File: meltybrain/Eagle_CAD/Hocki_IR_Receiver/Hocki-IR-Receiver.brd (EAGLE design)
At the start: 36 x 34 mm, 67 parts, among them U1 OPA2380AIDGKR, U10 LMH6612MAX/NOPB, U11 LMH6612MAX/NOPB, U2 OPA2380AIDGKR, U3 TLV3502AIDCNR, U4 TLV3502AIDCNR, U5 SN74LVC1G58DCKR, U6 NL27WZ32USG, U7 TMUX1204DGSR, U8 LP38693MP-5.0/NOPB, U9 TLV73310PDBVT

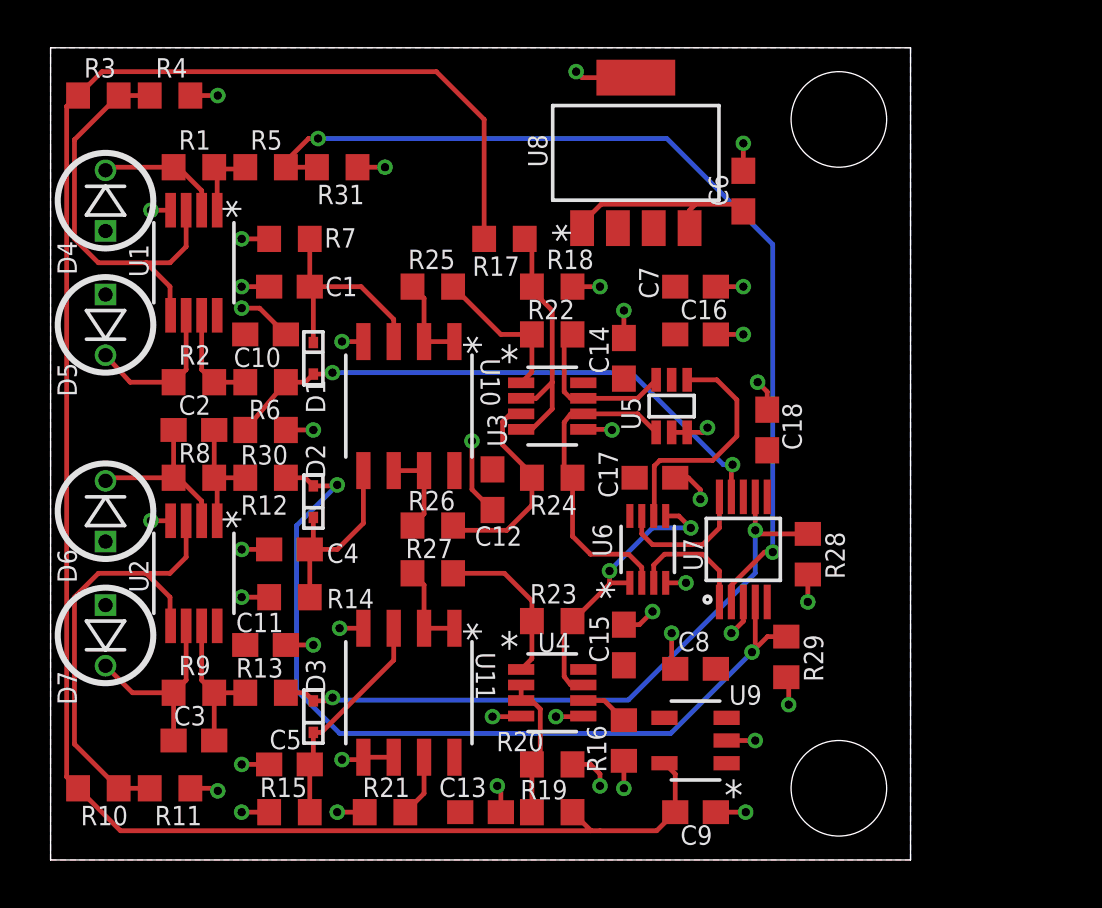
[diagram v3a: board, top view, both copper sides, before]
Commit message: updates
IR receiver should only be missing the connector
started layout for control...gave up...too late
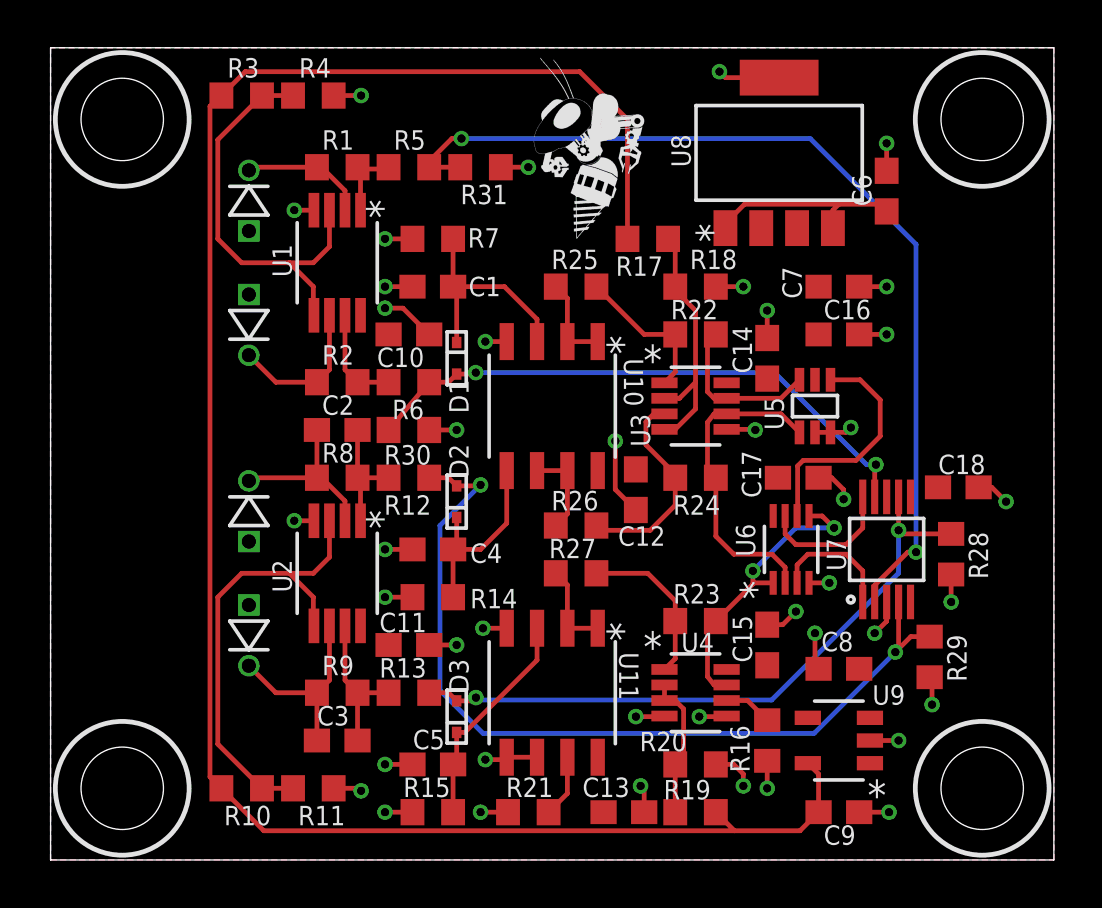
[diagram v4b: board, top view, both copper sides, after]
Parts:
- added U$1: (no value), RoboJackets-Aesthetics:ROBOBUZZ_0.4X
- added U$2: (no value), RoboJackets-Aesthetics:ROBOJACKETS
- moved C18 8.35 mm to (38.0, 15.6), turned to 0 degrees
- moved R28 6.00 mm to (37.7, 12.8)
- moved D4 6.00 mm to (8.30, 27.6), flipped to the bottom
- moved D5 6.00 mm to (8.30, 22.4), flipped to the bottom
- moved D6 6.00 mm to (8.30, 14.6), flipped to the bottom
- moved D7 6.00 mm to (8.30, 9.40), flipped to the bottom
- moved C1 6.00 mm to (16.0, 24.0)
- moved C10 6.00 mm to (15.0, 22.0)
- moved C11 6.00 mm to (15.0, 9.00)
- moved C12 6.00 mm to (24.5, 15.5)
- moved C13 6.00 mm to (24.0, 2.00)
- moved C14 6.00 mm to (30.0, 21.0)
- moved C15 6.00 mm to (30.0, 9.00)
- moved C16 6.00 mm to (33.0, 22.0)
- moved C17 6.00 mm to (31.3, 16.0)
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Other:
- board size 36 x 34 mm -> 42 x 34 mm
- board text added: "IR Receiver V1"

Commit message: progress...
IR receiver has all parts accounting BoM
started doing that for control
progress on control layout
Varun I hate this...
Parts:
- removed C4, C5: 50n, rcl:C0603
- removed R5: 50, resistor:R0603
- C1: value 50n -> 47n; device rcl:C0603 -> rcl:C1206
- C2: value 0.5p -> 47n; device rcl:C0603 -> rcl:C1206
- C3: value 2p -> 47n; device rcl:C0603 -> rcl:C1206
- R1: device resistor:R0603 -> rcl:R1206
- R10, R11, R16, R21, R28, R29, R3, R30, R31, R4: value 500 -> 499
- R14, R15, R7: value 30k -> 31.6k
- moved C2 7.07 mm to (17.0, 13.0), turned to 180 degrees
- moved R30 3.00 mm to (12.0, 18.0), turned to 0 degrees
- moved C1 2.00 mm to (18.0, 24.0)
- moved C3 2.00 mm to (14.0, 5.00), turned to 180 degrees
- moved R15 1.41 mm to (15.0, 3.00)
- moved R1 1.00 mm to (13.0, 29.0)
- moved R31 1.00 mm to (17.0, 29.0)
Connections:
- removed net N$11: C3.2, R13.1, R9.2, U2.7
- removed net N$8: C2.2, R12.1, R8.2, U2.1
- new net N$21: D1.2, R6.2
- net 100KGAIN: now also R12.1, R8.2, U2.1; no longer D2.2, R12.2
- net 100KPEAK: now also C2.1; no longer C4.1
- net 10KGAIN: now also R13.1, R9.2, U2.7; no longer D3.2, R13.2
- net 10KPEAK: now also C3.1; no longer C5.1
- net 10MGAIN: now also R1.2, U1.1; no longer R5.2
- net 1MGAIN: now also R2.2, R6.1, U1.7; no longer D1.2, R6.2
- net GND: now also C2.2, C3.2; no longer C4.2, C5.2
- net N$10: no longer C3.1
- net N$2: now also D2.2, R12.2; no longer R1.2, R5.1, U1.1
- net N$4: now also D3.2, R13.2; no longer R2.2, R6.1, U1.7
- net N$6: no longer C2.1
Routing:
- net N$11: track 6.32 -> 0.00 mm
- net 1MGAIN: track 24.5 -> 30.6 mm
- net 10KGAIN: track 27.5 -> 33.2 mm
- net N$8: track 5.15 -> 0.00 mm
- net N$4: track 4.32 -> 1.29 mm
- net 10MGAIN: track 40.4 -> 42.7 mm
- net N$10: track 8.34 -> 6.34 mm
- net N$6: track 7.31 -> 5.31 mm
- net N$2: track 3.11 -> 1.29 mm
- net 100KGAIN: track 36.7 -> 38.4 mm
- net GND: track 56.0 -> 57.7 mm
- net N$21: track 0.00 -> 1.29 mm
- net 10KPEAK: track 9.36 -> 9.88 mm

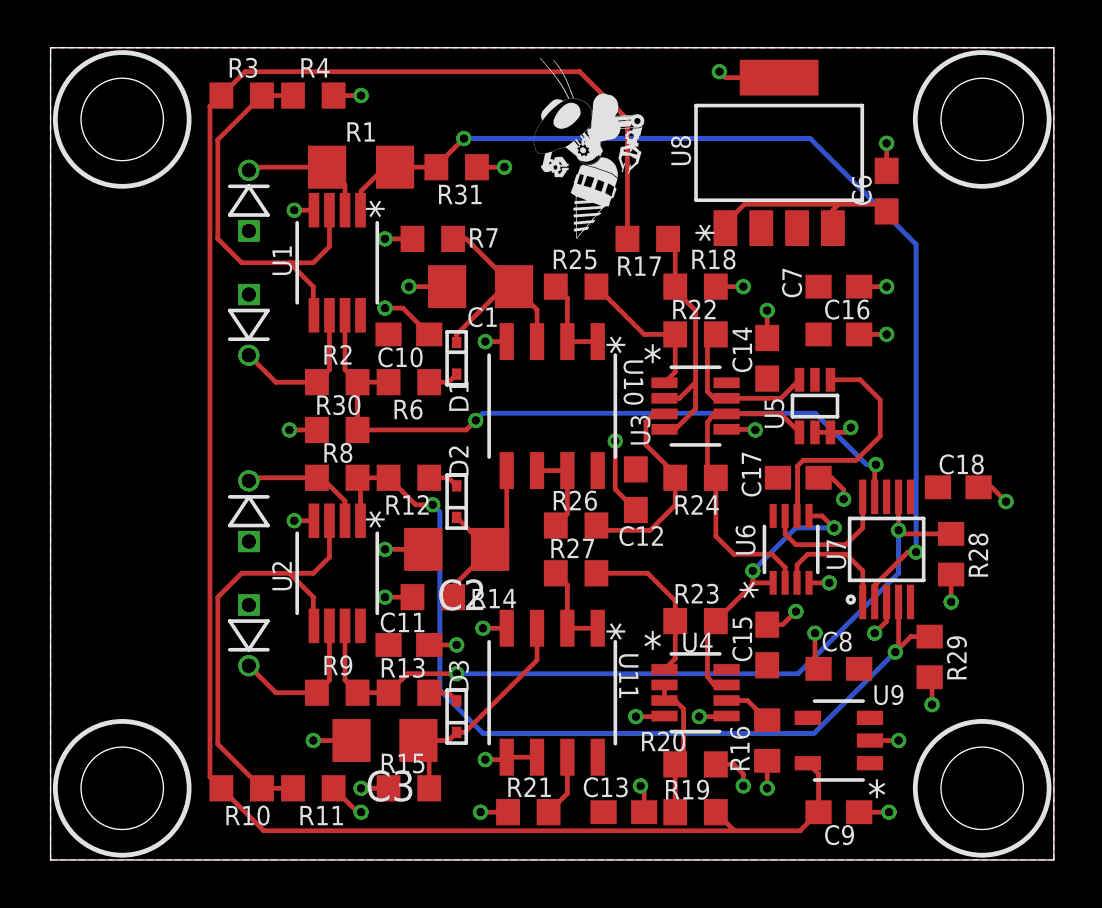
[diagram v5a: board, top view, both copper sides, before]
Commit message: added IR connectors
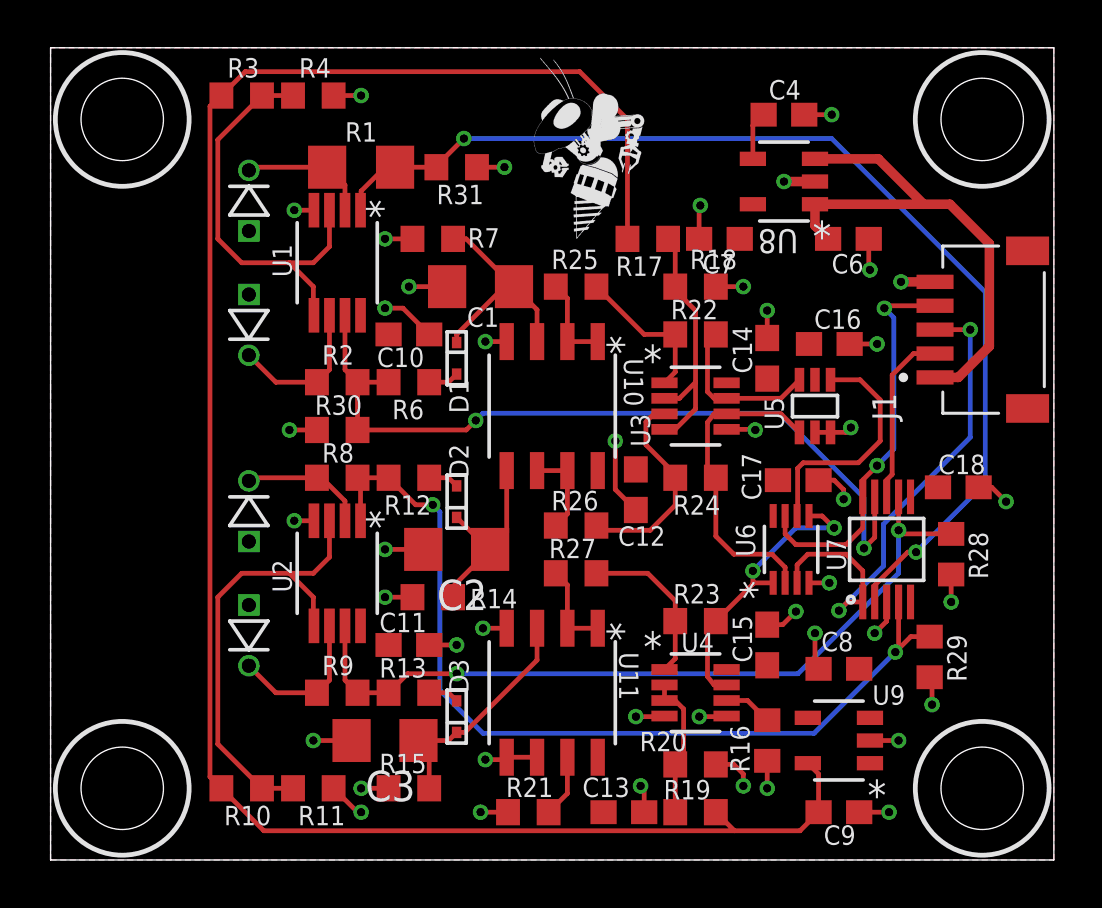
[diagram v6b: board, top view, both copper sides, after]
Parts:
- added C4: 100p, rcl:C0603
- added J1: SM05B-SRSS-TB(LF)(SN), Hocki_Library:SM05B-SRSS-TB(LF)(SN)
- C7: value 1u -> 2.2u
- U8: value LP38693MP-5.0/NOPB -> AP2210K-5.0TRG1; device Hocki_Library:SOT-223-5 -> Hocki_Library:SOT-23-5
- moved C7 5.39 mm to (28.0, 26.0), turned to 180 degrees
- moved C6 2.56 mm to (33.4, 26.0), turned to 0 degrees
- moved U8 1.22 mm to (30.7, 28.4), turned to 180 degrees
- moved C16 0.57 mm to (32.6, 21.6)
- moved C17 0.10 mm to (31.3, 15.9)
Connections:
- removed net VIN: C6.1, U8.1, U8.4
- new net 9V: C6.1, J1.1, U8.1, U8.3
- new net N$8: C4.1, U8.4
- net 5V: now also J1.S1, J1.S2, U8.5; no longer U8.3
- net A0: now also J1.3
- net A1: now also J1.4
- net GND: now also C4.2, J1.5, U8.2; no longer U8.5
- net VG_SIGNAL: now also J1.2
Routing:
- net 9V: track 0.00 -> 22.1 mm
- net A0: track 5.28 -> 21.9 mm, vias 0 -> 2
- net A1: track 5.78 -> 16.5 mm, vias 0 -> 2
- net VIN: track 8.51 -> 0.00 mm
- net VG_SIGNAL: track 0.00 -> 7.36 mm
- net 1MGAIN: track 30.6 -> 33.7 mm
- net 10MGAIN: track 42.7 -> 45.6 mm
- net N$8: track 0.00 -> 2.04 mm
- net GND: track 57.7 -> 59.4 mm, vias 42 -> 44

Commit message: 5 to 3 pin connector
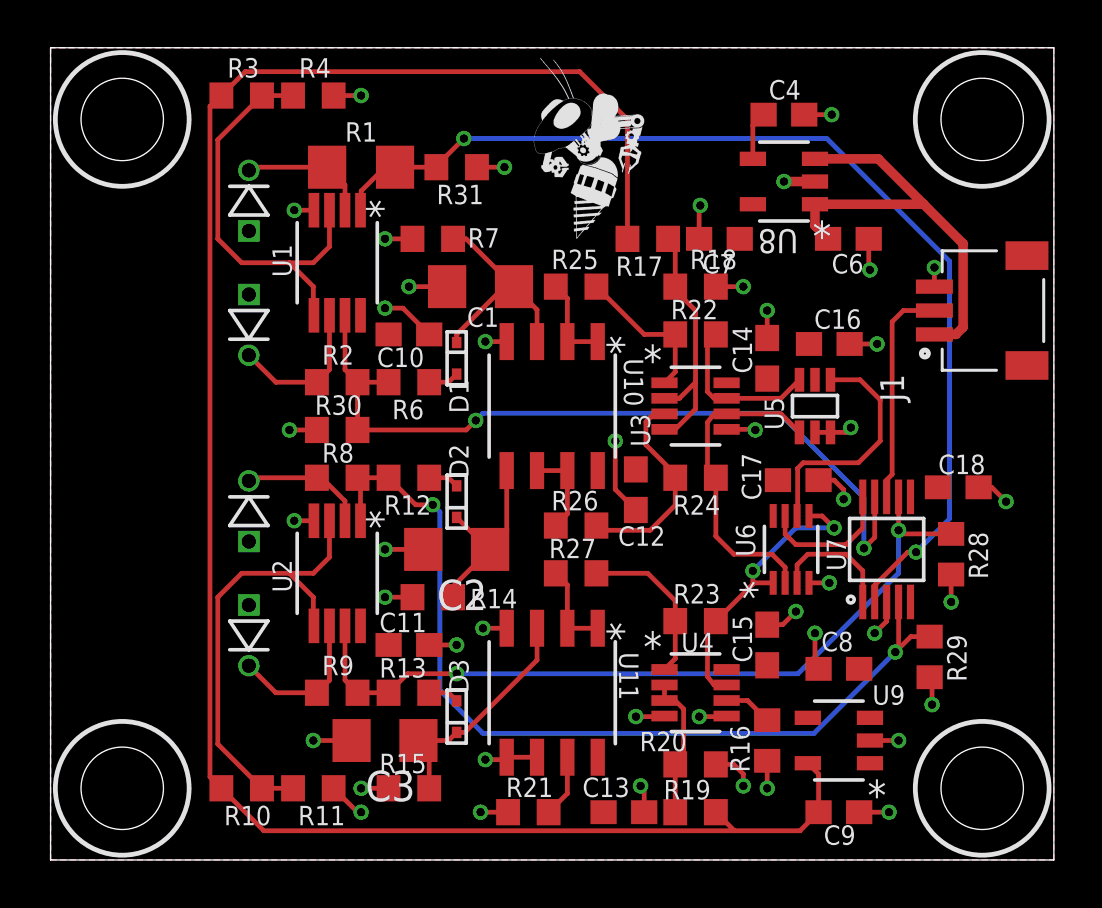
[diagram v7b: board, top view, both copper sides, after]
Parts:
- J1: value SM05B-SRSS-TB(LF)(SN) -> SM03B-SRSS-TB(LF)(SN); device Hocki_Library:SM05B-SRSS-TB(LF)(SN) -> Hocki_Library:SM03B-SRSS-TB(LF)(SN)
- moved J1 3.98 mm to (37.0, 23.0)
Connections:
- net A0: no longer J1.3
- net A1: no longer J1.4
- net GND: now also J1.3; no longer J1.5
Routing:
- net A0: track 21.9 -> 5.28 mm, vias 2 -> 0
- net A1: track 16.5 -> 5.78 mm, vias 2 -> 0
- net 9V: track 22.1 -> 18.7 mm
- net VG_SIGNAL: track 7.36 -> 9.39 mm
- net 10MGAIN: track 45.6 -> 44.3 mm
- net GND: track 59.4 -> 58.7 mm
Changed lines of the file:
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@@
 <attribute name="VALUE" x="30.065" y="29.295" size="1.27" layer="27"/>
 </element>
-<element name="J1" library="Hocki_Library" package="SM05B-SRSS-TB(LF)(SN)" value="SM05B-SRSS-TB(LF)(SN)" x="40.9" y="22.2" smashed="yes" rot="R90">
-<attribute name="DKPN" value="455-1805-1-ND" x="40.9" y="22.2" size="1.778" layer="27" rot="R90" display="off"/>
-<attribute name="NAME" x="35.4" y="18.4" size="1" layer="25" font="vector" rot="R90"/>
-<attribute name="VALUE" x="42.4" y="18.7" size="1" layer="27" font="vector" rot="R90" align="top-left"/>
+<element name="J1" library="Hocki_Library" package="SM03B-SRSS-TB(LF)(SN)" value="SM03B-SRSS-TB(LF)(SN)" x="37" y="23" smashed="yes" rot="R90">
+<attribute name="DKPN" value="455-1803-1-ND" x="37" y="23" size="1.778" layer="27" rot="R90" display="off"/>
+<attribute name="NAME" x="35.73" y="19.19" size="1" layer="25" font="vector" rot="R90"/>
+<attribute name="VALUE" x="42.35" y="19.19" size="1" layer="27" font="vector" rot="R90" align="top-left"/>
 </element>
 </elements>
@@
 <wire x1="32" y1="28.4" x2="30.7" y2="28.4" width="0.4" layer="1"/>
 <via x="30.7" y="28.4" extent="1-16" drill="0.35"/>
-<contactref element="J1" pad="5"/>
-<wire x1="37.025" y1="24.2" x2="35.6" y2="24.2" width="0.4" layer="1"/>
-<via x="35.6" y="24.2" extent="1-16" drill="0.35"/>
+<contactref element="J1" pad="3"/>
+<wire x1="37" y1="24" x2="37" y2="24.8" width="0.2" layer="1"/>
+<via x="37" y="24.8" extent="1-16" drill="0.35"/>
 </signal>
 <signal name="5V">
@@
 <contactref element="C18" pad="1"/>
 <contactref element="U8" pad="5"/>
+<contactref element="J1" pad="S2"/>
 <contactref element="J1" pad="S1"/>
-<contactref element="J1" pad="S2"/>
 </signal>
 <signal name="1MGAIN">
@@
 <wire x1="35.88615" y1="12.88615" x2="36.2306" y2="12.88615" width="0.2" layer="1"/>
 <via x="36.2306" y="12.88615" extent="1-16" drill="0.35"/>
-<wire x1="36.2306" y1="12.88615" x2="39.1306" y2="15.78615" width="0.2" layer="16"/>
-<wire x1="39.1306" y1="23.7694" x2="39.1306" y2="15.78615" width="0.2" layer="16"/>
-<wire x1="32.7" y1="30.2" x2="17.3" y2="30.2" width="0.2" layer="16"/>
+<wire x1="36.2306" y1="12.88615" x2="37.6306" y2="14.28615" width="0.2" layer="16"/>
+<wire x1="37.6306" y1="25.0694" x2="37.6306" y2="14.28615" width="0.2" layer="16"/>
+<wire x1="32.5" y1="30.2" x2="17.3" y2="30.2" width="0.2" layer="16"/>
 <via x="17.3" y="30.2" extent="1-16" drill="0.35"/>
 <wire x1="17.3" y1="30.2" x2="16.15" y2="29.05" width="0.2" layer="1"/>
 <wire x1="16.15" y1="29" x2="16.15" y2="29.05" width="0.2" layer="1"/>
 <wire x1="34.5" y1="11.5" x2="35.88615" y2="12.88615" width="0.2" layer="1"/>
-<wire x1="39.1306" y1="23.7694" x2="32.7" y2="30.2" width="0.2" layer="16"/>
+<wire x1="37.6306" y1="25.0694" x2="32.5" y2="30.2" width="0.2" layer="16"/>
 <contactref element="R31" pad="2"/>
 <contactref element="U1" pad="1"/>
@@
 <wire x1="34" y1="13.9" x2="33.3" y2="13.2" width="0.2" layer="1"/>
 <wire x1="34" y1="15.2" x2="34" y2="13.9" width="0.2" layer="1"/>
-<wire x1="34" y1="15.2" x2="34" y2="15.9064" width="0.2" layer="1"/>
-<wire x1="34" y1="15.9064" x2="34.6" y2="16.5064" width="0.2" layer="1"/>
-<via x="34.6" y="16.5064" extent="1-16" drill="0.35"/>
-<via x="34.904096875" y="23.095903125" extent="1-16" drill="0.35"/>
-<wire x1="34.904096875" y1="23.095903125" x2="35.3" y2="22.7" width="0.2" layer="16"/>
-<wire x1="34.6" y1="16.5064" x2="35.3" y2="17.2064" width="0.2" layer="16"/>
-<wire x1="35.3" y1="22.7" x2="35.3" y2="17.2064" width="0.2" layer="16"/>
-<contactref element="J1" pad="4"/>
-<wire x1="34.904096875" y1="23.095903125" x2="35.00819375" y2="23.2" width="0.2" layer="1"/>
-<wire x1="35.00819375" y1="23.2" x2="37.025" y2="23.2" width="0.2" layer="1"/>
 </signal>
 <signal name="A0">
@@
 <wire x1="33.3" y1="12.8" x2="34" y2="12.1" width="0.2" layer="1"/>
 <wire x1="34" y1="12.1" x2="34" y2="10.8" width="0.2" layer="1"/>
-<contactref element="J1" pad="3"/>
-<wire x1="34" y1="10.8" x2="33.3628" y2="10.8" width="0.2" layer="1"/>
-<wire x1="33.3628" y1="10.8" x2="33" y2="10.4372" width="0.2" layer="1"/>
-<via x="33" y="10.4372" extent="1-16" drill="0.35"/>
-<via x="38.5" y="22.2" extent="1-16" drill="0.35"/>
-<wire x1="33" y1="10.4372" x2="34.8694" y2="12.3066" width="0.2" layer="16"/>
-<wire x1="38.5" y1="17.69180625" x2="38.5" y2="22.2" width="0.2" layer="16"/>
-<wire x1="34.8694" y1="12.3066" x2="34.8694" y2="14.06120625" width="0.2" layer="16"/>
-<wire x1="34.8694" y1="14.06120625" x2="38.5" y2="17.69180625" width="0.2" layer="16"/>
-<wire x1="37.025" y1="22.2" x2="38.5" y2="22.2" width="0.2" layer="1"/>
 </signal>
 <signal name="N$13">
@@
 <wire x1="35" y1="15.2" x2="35" y2="15.90819375" width="0.2" layer="1"/>
 <wire x1="35" y1="15.90819375" x2="35.2306" y2="16.13879375" width="0.2" layer="1"/>
-<wire x1="35.2306" y1="16.13879375" x2="35.2306" y2="20.3" width="0.2" layer="1"/>
+<wire x1="35.2306" y1="16.13879375" x2="35.2306" y2="22.5306" width="0.2" layer="1"/>
 <contactref element="J1" pad="2"/>
-<wire x1="37.025" y1="21.2" x2="36.1306" y2="21.2" width="0.2" layer="1"/>
-<wire x1="36.1306" y1="21.2" x2="35.2306" y2="20.3" width="0.2" layer="1"/>
+<wire x1="37" y1="23" x2="35.7" y2="23" width="0.2" layer="1"/>
+<wire x1="35.7" y1="23" x2="35.2306" y2="22.5306" width="0.2" layer="1"/>
 </signal>
 <signal name="N$17">
@@
 <contactref element="U8" pad="1"/>
 <contactref element="U8" pad="3"/>
-<contactref element="J1" pad="1"/>
-<wire x1="37.025" y1="20.2" x2="38" y2="20.2" width="0.4" layer="1"/>
-<wire x1="38" y1="20.2" x2="39.3" y2="21.5" width="0.4" layer="1"/>
-<wire x1="39.3" y1="21.5" x2="39.3" y2="25.8" width="0.4" layer="1"/>
+<wire x1="38.2" y1="22.3" x2="38.2" y2="25.8" width="0.4" layer="1"/>
 <wire x1="32" y1="27.45" x2="36.55" y2="27.45" width="0.4" layer="1"/>
-<wire x1="36.55" y1="27.45" x2="37.65" y2="27.45" width="0.4" layer="1"/>
-<wire x1="39.3" y1="25.8" x2="37.65" y2="27.45" width="0.4" layer="1"/>
+<wire x1="38.2" y1="25.8" x2="36.55" y2="27.45" width="0.4" layer="1"/>
 <wire x1="32.55" y1="26" x2="32" y2="26.55" width="0.4" layer="1"/>
 <wire x1="32" y1="26.55" x2="32" y2="27.45" width="0.4" layer="1"/>
 <wire x1="36.55" y1="27.45" x2="34.65" y2="29.35" width="0.4" layer="1"/>
 <wire x1="34.65" y1="29.35" x2="32" y2="29.35" width="0.4" layer="1"/>
+<contactref element="J1" pad="1"/>
+<wire x1="37" y1="22" x2="37.9" y2="22" width="0.4" layer="1"/>
+<wire x1="37.9" y1="22" x2="38.2" y2="22.3" width="0.4" layer="1"/>
 </signal>
 </signals>
